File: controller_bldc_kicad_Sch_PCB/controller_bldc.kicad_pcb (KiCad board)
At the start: 2 copper layers, 178.1 x 101.9 mm, 55 parts, among them J1 Battery Supply, J2 Emergency Button OUT, J3 Emergency Button IN, J4 Brake, J5 Throttle, J6 LM35, J7 Hall Sensors, J8 Nextion Nx3224T028, J9 BLDC Motor, K1 ADW11, Q1 IRF1010N, Q2 IRF1010N, Q3 IRF1010N, Q4 IRF1010N, Q5 IRF1010N, Q6 IRF1010N, SW1 SW_SPST, SW2 SW_Push, U1 ESP32-DEVKITC-32D, U2 LM317_TO-220, U3 LM7805_TO220, U4 IR2103, U8 IR2103, U9 IR2103

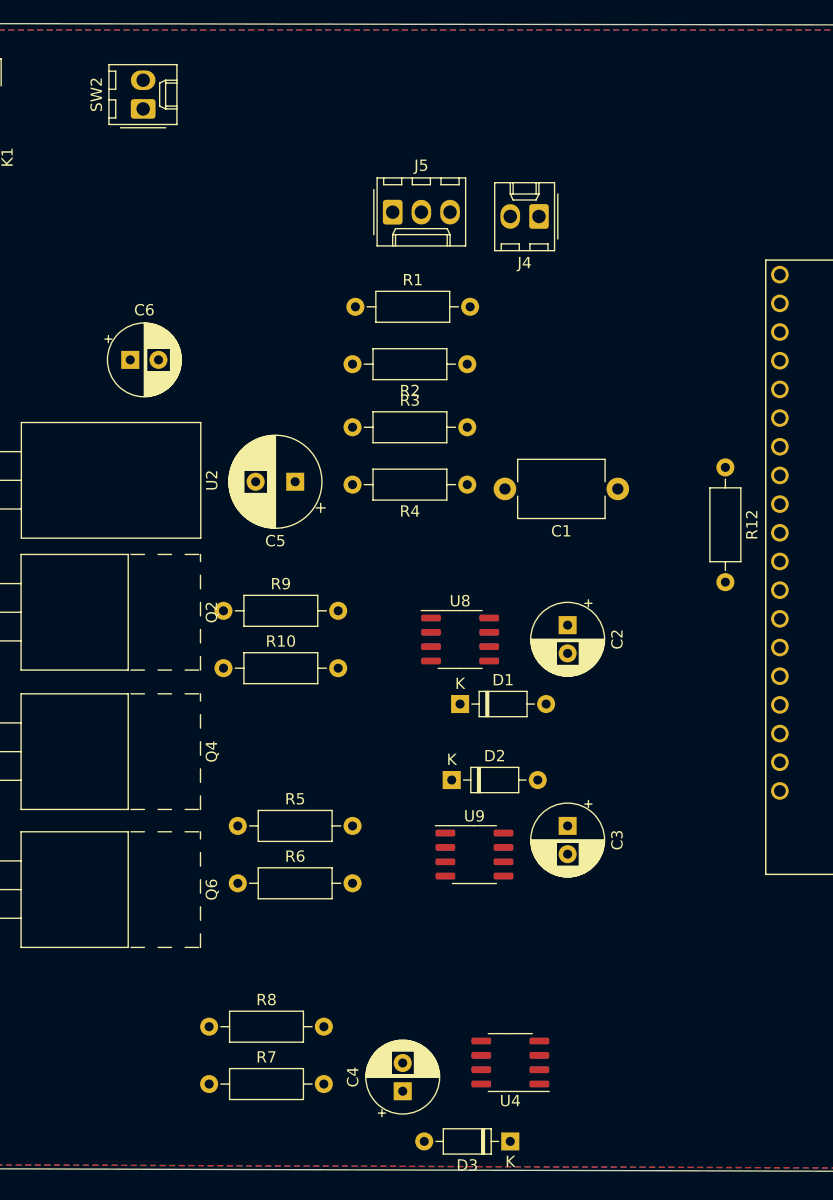
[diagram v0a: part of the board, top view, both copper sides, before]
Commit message: Fix in the IR2103 group arrangements inside the PCB
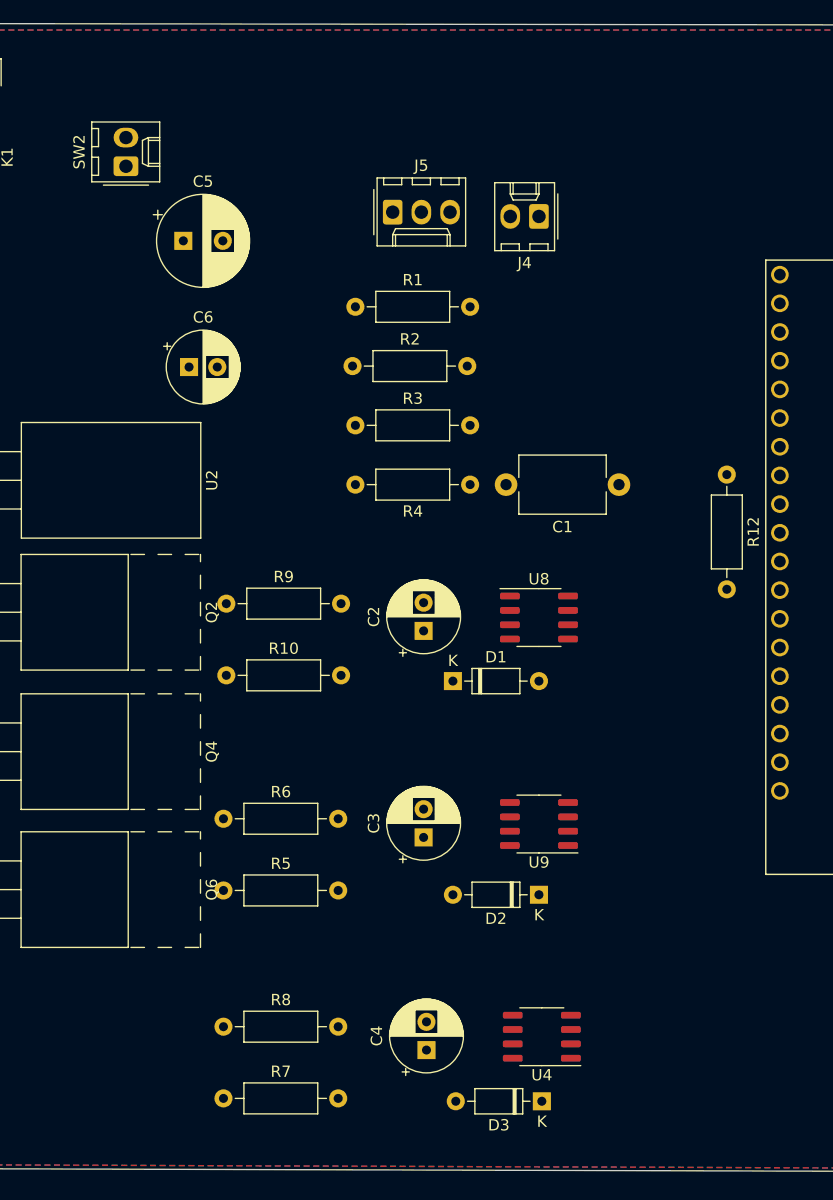
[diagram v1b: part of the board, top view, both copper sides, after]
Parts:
- moved C5 23.5 mm to (167.9, 94.2), turned to 0 degrees
- moved C3 12.8 mm to (189.2, 147.1), turned to 90 degrees
- moved C2 12.8 mm to (189.2, 128.8), turned to 90 degrees
- moved D2 12.8 mm to (199.4, 152.1), turned to 180 degrees
- moved R2 10.2 mm to (182.9, 105.3), turned to 0 degrees
- moved U8 7.25 mm to (199.4, 127.6)
- moved U9 6.32 mm to (199.4, 145.9), turned to 180 degrees
- moved R6 5.85 mm to (171.4, 145.4)
- moved R5 5.85 mm to (171.4, 151.8)
- moved SW2 5.30 mm to (162.8, 87.6)
- moved C6 5.25 mm to (168.4, 105.4)
- moved D3 4.52 mm to (199.6, 170.4)
- moved C4 4.21 mm to (189.4, 165.9)
- moved U4 3.61 mm to (199.6, 164.7)
- moved D1 2.13 mm to (191.8, 133.2)
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
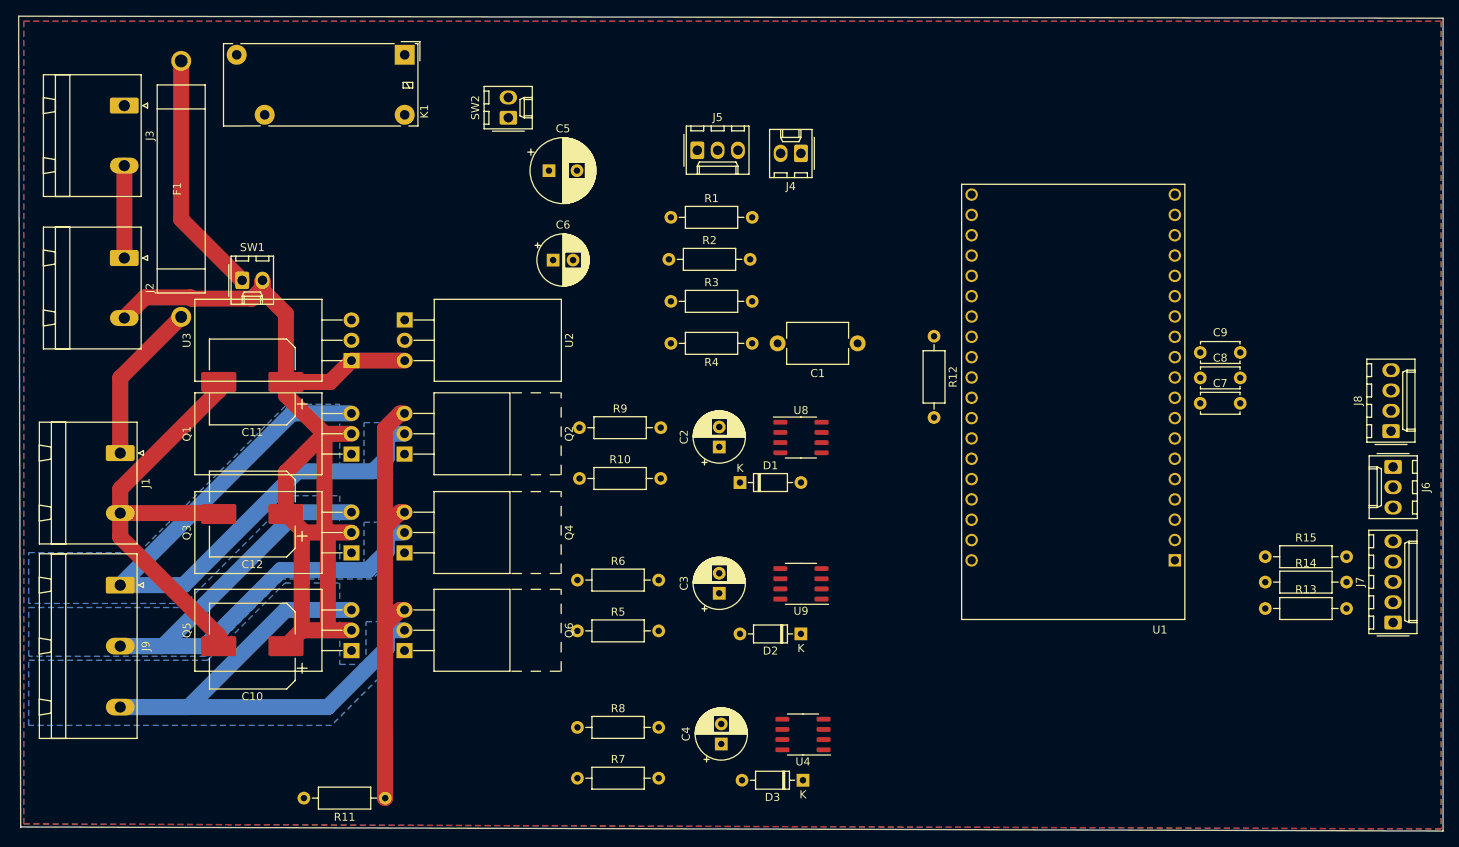
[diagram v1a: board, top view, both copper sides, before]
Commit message: PCB in v0.7, only relay to change for next and maybe the first tri
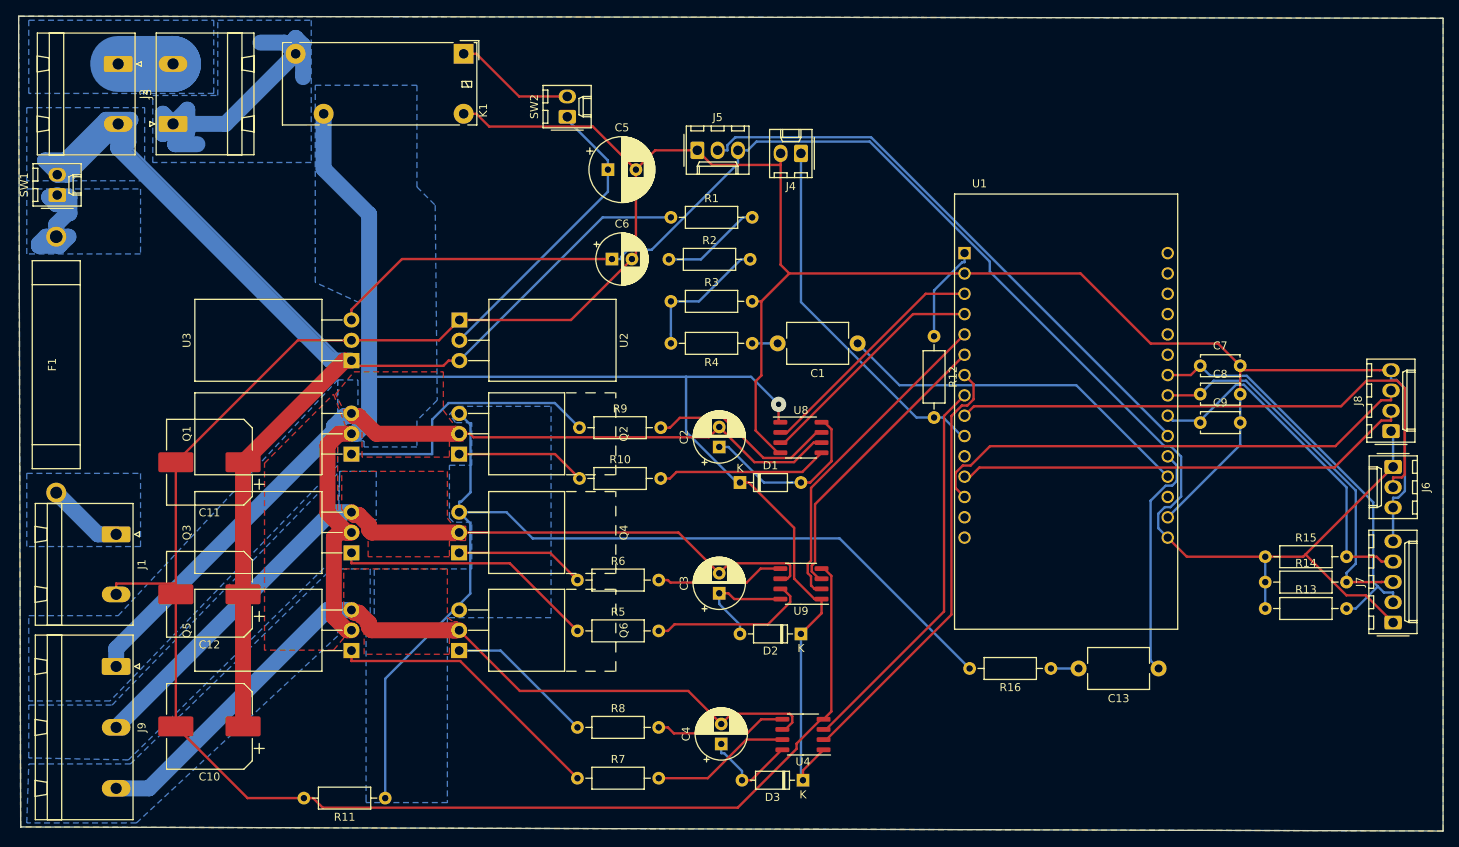
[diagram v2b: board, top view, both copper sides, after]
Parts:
- added C13: 0.1uF, Capacitor_THT:C_Disc_D7.5mm_W5.0mm_P10.00mm, F.Cu at (244.1, 156.5)
- added R16: 2.2k, Resistor_THT:R_Axial_DIN0207_L6.3mm_D2.5mm_P10.16mm_Horizontal, F.Cu at (230.6, 156.5)
- U1: footprint MODULE_ESP32-DEVKITC-32D -> ESP32-DEVKITC-32D_Electeam:MODULE_ESP32-DEVKITC-32D
- moved F1 27.0 mm to (106.3, 118.5)
- moved SW1 25.5 mm to (106.4, 97.3), turned to 90 degrees
- moved J2 24.3 mm to (114.0, 80.9)
- moved C10 11.4 mm to (125.5, 163.7)
- moved C12 11.4 mm to (125.5, 147.2)
- moved C11 11.4 mm to (125.5, 130.7)
- moved J1 10.2 mm to (113.8, 139.7)
- moved J9 10.2 mm to (113.8, 156.2)
- moved C9 8.76 mm to (249.3, 125.7)
- moved C6 7.37 mm to (175.8, 105.3)
- moved SW2 7.37 mm to (170.2, 87.5)
- moved C5 7.37 mm to (175.3, 94.1)
- moved K1 7.37 mm to (157.2, 79.6)
- moved U2 6.83 mm to (156.7, 112.9)
- moved Q4 6.83 mm to (156.7, 142.0)
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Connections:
- D1 pad 1: +36V -> 36V-Power
- D2 pad 1: +36V -> 36V-Power
- D3 pad 1: +36V -> 36V-Power
- Q1 pad 2: +36V -> 36V-Power
- Q3 pad 2: +36V -> 36V-Power
- Q5 pad 2: +36V -> 36V-Power
- U1 pad 10: HALL-B -> Brake
- U1 pad 11: HALL-C -> (no net)
- U1 pad 12: Throttle -> TX-LCD
- U1 pad 13: Current_Sensor -> RX-LCD
- U1 pad 15: Voltage_Sensor -> (no net)
- U1 pad 16: Net-(U1-Pad16) -> (no net)
- U1 pad 17: Net-(U1-Pad17) -> (no net)
- U1 pad 18: Net-(U1-Pad18) -> (no net)
- U1 pad 19: +5V -> (no net)
- U1 pad 2: Net-(U1-Pad2) -> GND
- U1 pad 20: GND -> (no net)
- U1 pad 21: Net-(U1-Pad21) -> (no net)
- U1 pad 22: Net-(U1-Pad22) -> HALL-A
- U1 pad 23: RX-LCD -> HALL-B
- U1 pad 24: TX-LCD -> HALL-C
- U1 pad 25: Net-(U1-Pad25) -> Throttle
- U1 pad 26: Net-(U1-Pad26) -> Current_Sensor_IN
- U1 pad 27: Brake -> Voltage_Sensor
- U1 pad 28: LM35 -> (no net)
- U1 pad 29: LIN3 -> GND
- U1 pad 3: Net-(U1-Pad3) -> HIN1
- U1 pad 30: HIN3 -> +5V
- U1 pad 4: Net-(U1-Pad4) -> LIN1
- U1 pad 5: Net-(U1-Pad5) -> HIN2
- U1 pad 6: Net-(U1-Pad6) -> LIN2
- U1 pad 7: Net-(U1-Pad7) -> HIN3
- U1 pad 8: Net-(U1-Pad8) -> LIN3
- U1 pad 9: HALL-A -> LM35
- U4 pad 1: +36V -> 36V-Power
- U8 pad 1: +36V -> 36V-Power
- U9 pad 1: +36V -> 36V-Power
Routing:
- net GND: track 55.6 -> 443.5 mm
- net +5V: track 0.00 -> 203.4 mm
- net 36V-Power: track 0.00 -> 194.8 mm, vias 0 -> 1
- net +36V: track 129.6 -> 243.0 mm
- net Throttle: track 0.00 -> 72.9 mm
- net LM35: track 0.00 -> 70.8 mm
- net Current_Sensor: track 62.4 -> 126.9 mm
- net RX-LCD: track 0.00 -> 62.9 mm
- net TX-LCD: track 0.00 -> 57.4 mm
- net HIN3: track 0.00 -> 54.4 mm
- net HALL-A: track 0.00 -> 52.5 mm
- net LIN3: track 0.00 -> 49.2 mm
- net HALL-B: track 0.00 -> 47.7 mm
- net Net-(J3-Pad1): track 0.00 -> 47.6 mm
- net Brake: track 0.00 -> 46.0 mm
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- added copper zone on B.Cu, net +36V
- added copper zone on B.Cu, net 36V-Power
- added copper zone on F.Cu, net 36V-Power
- added copper zone on B.Cu, net Current_Sensor
- added copper zone on B.Cu, net Net-(F1-Pad1)
- added copper zone on B.Cu, net Net-(F1-Pad2)
- added copper zone on B.Cu, net Net-(J2-Pad1)
- added copper zone on B.Cu, net Net-(J3-Pad1)
- added copper zone on F.Cu, net PH1
- added copper zone on F.Cu, net PH2
- added copper zone on F.Cu, net PH3

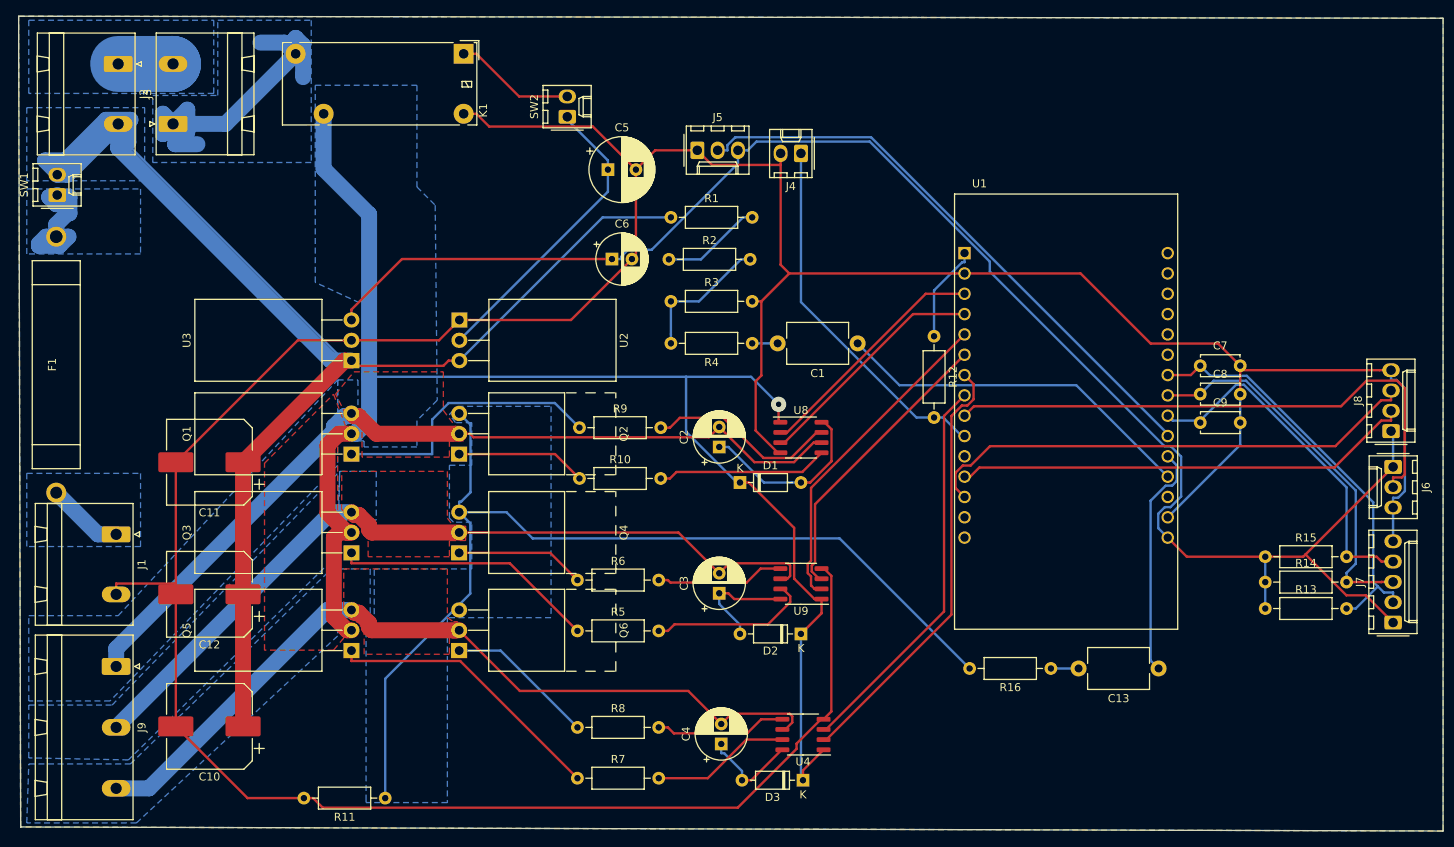
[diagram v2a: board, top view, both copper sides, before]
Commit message: V0.8 with everything except for the relay that should consume less current, 36V-Power is fixed.
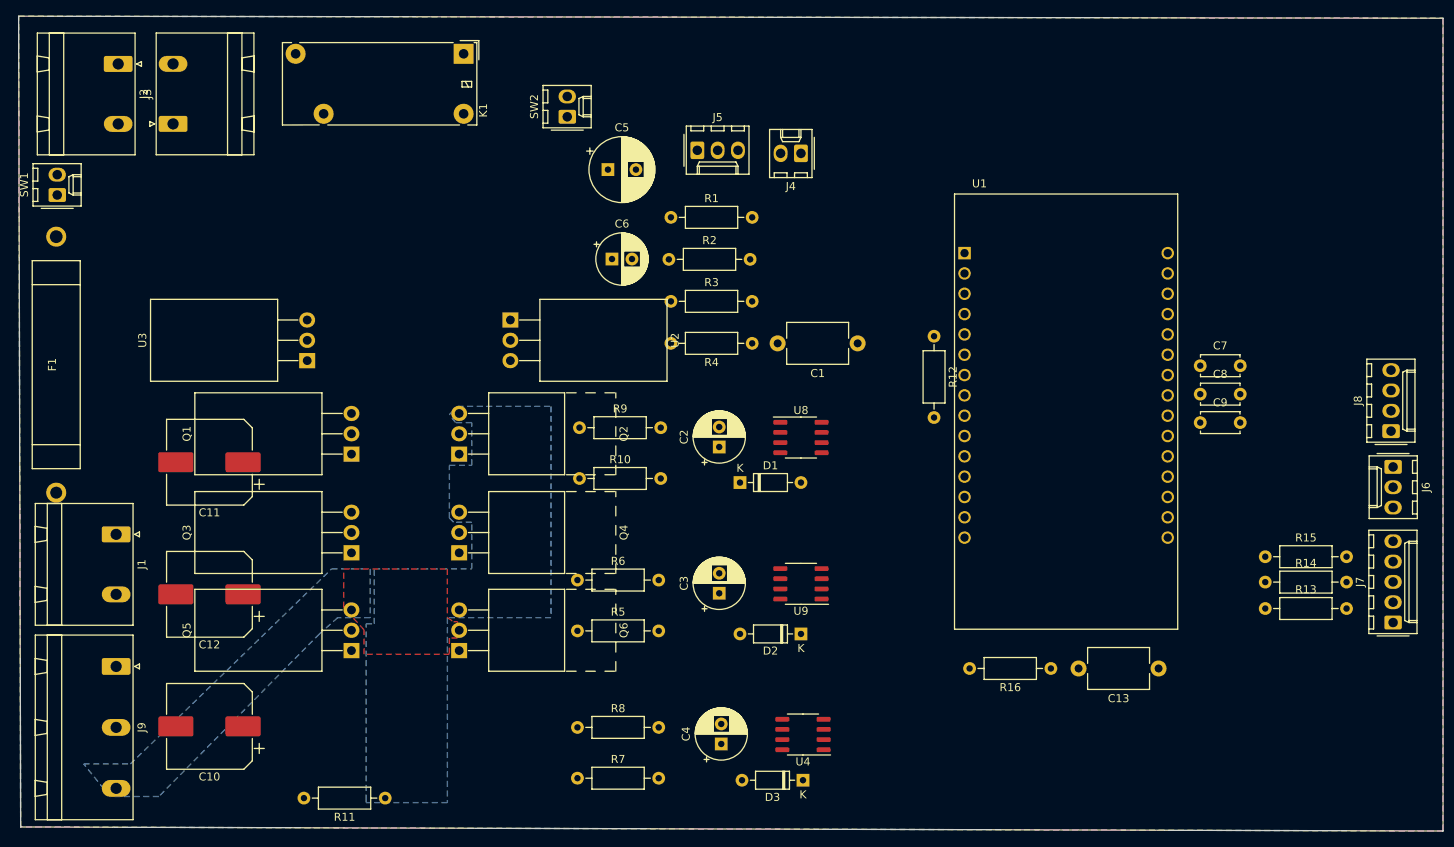
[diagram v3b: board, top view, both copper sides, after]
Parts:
- SW1: value SW_SPST -> ON_OFF
- SW2: value SW_Push -> OPC
- moved U2 6.38 mm to (163.1, 112.9)
- moved U3 5.54 mm to (137.7, 118.0)
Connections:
- D1 pad 1: 36V-Power -> +12V
- D2 pad 1: 36V-Power -> +12V
- D3 pad 1: 36V-Power -> +12V
- U4 pad 1: 36V-Power -> +12V
- U8 pad 1: 36V-Power -> +12V
- U9 pad 1: 36V-Power -> +12V
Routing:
- net GND: track 443.5 -> 0.00 mm
- net +36V: track 243.0 -> 0.00 mm
- net +5V: track 203.4 -> 0.00 mm
- net 36V-Power: track 194.8 -> 0.00 mm, vias 1 -> 0
- net Current_Sensor: track 126.9 -> 0.00 mm
- net PH1: track 107.5 -> 0.00 mm
- net PH3: track 103.0 -> 0.00 mm
- net PH2: track 102.2 -> 0.00 mm
- net Throttle: track 72.9 -> 0.00 mm
- net LM35: track 70.8 -> 0.00 mm
- net RX-LCD: track 62.9 -> 0.00 mm
- net TX-LCD: track 57.4 -> 0.00 mm
- net HIN3: track 54.4 -> 0.00 mm
- net HALL-A: track 52.5 -> 0.00 mm
- net LIN3: track 49.2 -> 0.00 mm
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- removed copper zone on B.Cu, net +36V
- removed copper zone on B.Cu, net 36V-Power
- removed copper zone on F.Cu, net 36V-Power
- removed copper zone on B.Cu, net Net-(F1-Pad1)
- removed copper zone on B.Cu, net Net-(F1-Pad2)
- removed copper zone on B.Cu, net Net-(J2-Pad1)
- removed copper zone on B.Cu, net Net-(J3-Pad1)
- removed copper zone on B.Cu, net PH1
- removed copper zone on F.Cu, net PH1
- removed copper zone on B.Cu, net PH2
- removed copper zone on F.Cu, net PH2
